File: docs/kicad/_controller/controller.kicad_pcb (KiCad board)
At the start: 2 copper layers, 134.6 x 104.1 mm, 88 parts, among them J1 24V, J10 bbb, J11 Y, J12 X_ZERO, J13 Z, J14 WS2812B Strip, J15 Display, J16 X_LIM, J17 Y_ZERO, J18 Y_LIM, J19 Z_ZERO, J2 GND, J20 Z_LIM, J21 PROBE, J22 UNUSED, J3 GND, J4 5V, J5 SPIN, J6 bbb, J7 X, J8 bbb, J9 bbb, M1 A4988, M2 A4988, M3 A4988, M4 SD_TYP0, U1 ESP32_DEV_0, U2 74HC165

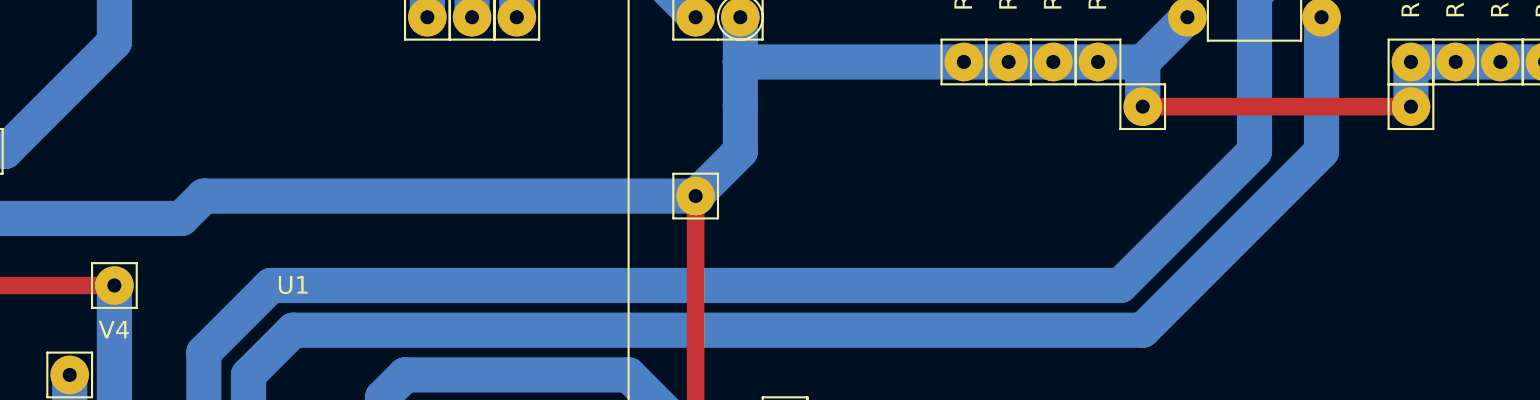
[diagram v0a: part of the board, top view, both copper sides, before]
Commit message: added capacitor and tested I2SI on cnc3018
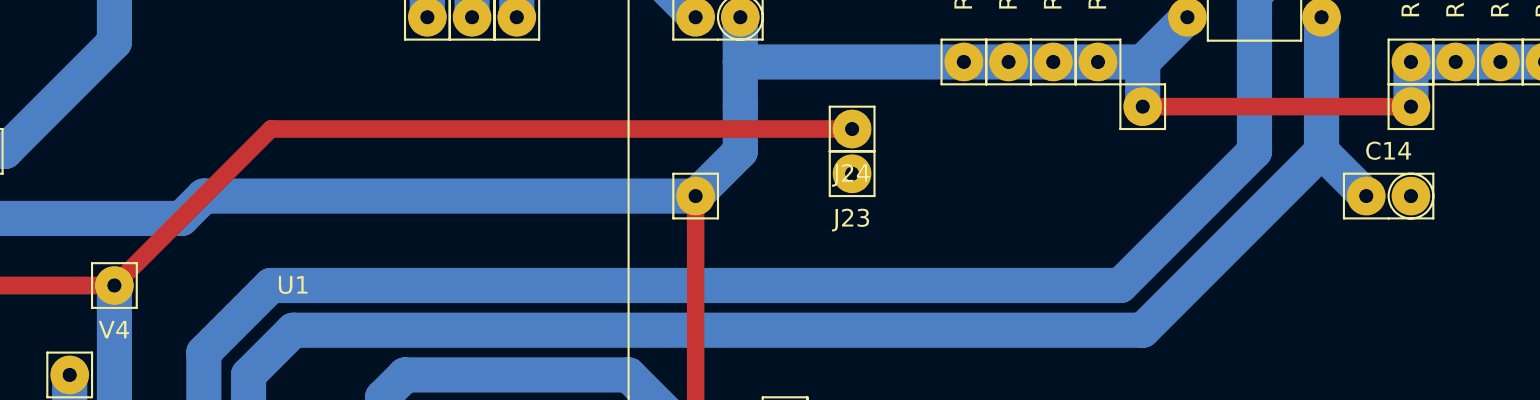
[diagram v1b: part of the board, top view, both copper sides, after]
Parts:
- added C14: 472nf, cnc3018-PCB:my2pin, F.Cu at (116.8, -33.0)
- added J23: GND, cnc3018-PCB:my1pin, F.Cu at (85.1, -34.3)
- added J24: SPIN, cnc3018-PCB:my1pin, F.Cu at (85.1, -36.8)
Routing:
- net Net-(J24-Pad1): track 78.3 -> 123.9 mm
- net Net-(C14-Pad2): track 76.4 -> 80.0 mm

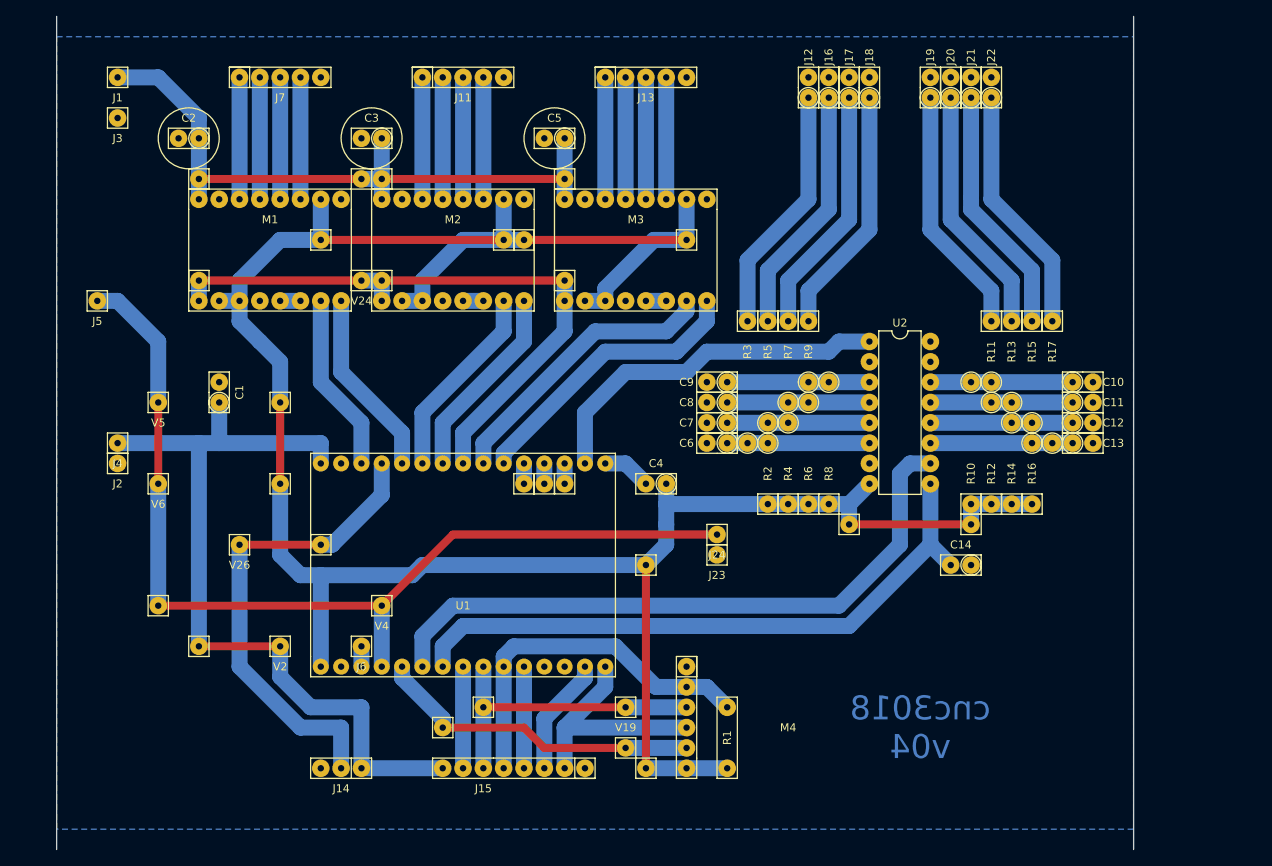
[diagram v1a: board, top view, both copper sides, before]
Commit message: kicad controller board v2.0 and smaller lcd_connector
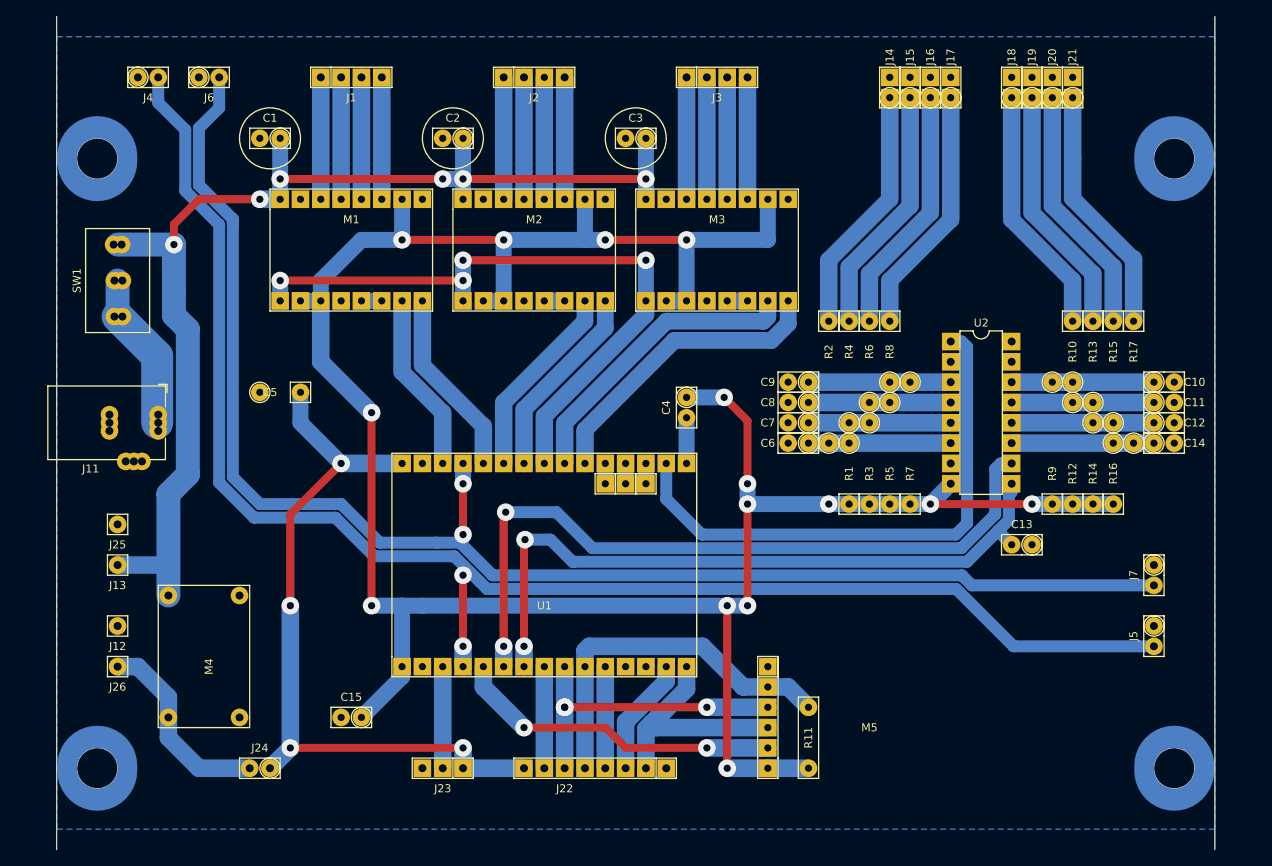
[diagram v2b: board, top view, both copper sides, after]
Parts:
- removed V1: v30, cnc3018-PCB:my1pin
- removed V10: v17, cnc3018-PCB:my1pin
- removed V11: v18, cnc3018-PCB:my1pin
- removed V12: v19, cnc3018-PCB:my1pin
- removed V13: v10, cnc3018-PCB:my1pin
- removed V14: v00, cnc3018-PCB:my1pin
- removed V15: v20, cnc3018-PCB:my1pin
- removed V16: v60, cnc3018-PCB:my1pin
- removed V17: v61, cnc3018-PCB:my1pin
- removed V18: v70, cnc3018-PCB:my1pin
- removed V19: v71, cnc3018-PCB:my1pin
- removed V2: v31, cnc3018-PCB:my1pin
- removed V20: v01, cnc3018-PCB:my1pin
- removed V21: v11, cnc3018-PCB:my1pin
- removed V22: v12, cnc3018-PCB:my1pin
- removed V23: v02, cnc3018-PCB:my1pin
- removed V24: v21, cnc3018-PCB:my1pin
- removed V25: v22, cnc3018-PCB:my1pin
- removed V26: v50, cnc3018-PCB:my1pin
- removed V27: v51, cnc3018-PCB:my1pin
- removed V28: v13, cnc3018-PCB:my1pin
- removed V29: v23, cnc3018-PCB:my1pin
- removed V3: v40, cnc3018-PCB:my1pin
- removed V30: v03, cnc3018-PCB:my1pin
- removed V4: v41, cnc3018-PCB:my1pin
- removed V5: v42, cnc3018-PCB:my1pin
- removed V6: v43, cnc3018-PCB:my1pin
- removed V7: v14, cnc3018-PCB:my1pin
- removed V8: v15, cnc3018-PCB:my1pin
- removed V9: v16, cnc3018-PCB:my1pin
- added C15: 220uf 10V, cnc3018-PCB:my2pin, F.Cu at (40.6, -14.0)
- added J25: bbb, cnc3018-PCB:my1pin, F.Cu at (10.2, -38.1)
- added J26: bbb, cnc3018-PCB:my1pin, F.Cu at (10.2, -20.3)
- added M5: SD_TYP0, cnc3018-PCB:my6Pin, F.Cu at (91.4, -20.3)
- added SW1: POWER, cnc3018-PCB:SW_DPDT_BLUE_LEVER, F.Cu at (10.2, -68.6)
- C1: value 33uf -> 100uf
- C13: value 100nf -> 472nf
- C14: value 472nf -> 100nf
- C5: value 100uf -> 330uf 50v; footprint cnc3018-PCB:my2pin -> cnc3018-PCB:mySkip1
- J1: value 24V -> X_AXIS; footprint cnc3018-PCB:my1pin -> cnc3018-PCB:my4pin
- J11: value Y -> Jack-DC; footprint cnc3018-PCB:my5Pin -> cnc3018-PCB:myBarrelJack
- J12: value X_ZERO -> bbb; footprint cnc3018-PCB:my2pin -> cnc3018-PCB:my1pin
- J13: value Z -> bbb; footprint cnc3018-PCB:my5Pin -> cnc3018-PCB:my1pin
- J14: value WS2812B Strip -> X_ZERO; footprint cnc3018-PCB:my3pin -> cnc3018-PCB:my2pin
- J15: value Display -> X_LIM; footprint cnc3018-PCB:my8Pin -> cnc3018-PCB:my2pin
- J16: value X_LIM -> Y_ZERO
- J17: value Y_ZERO -> Y_LIM
- J18: value Y_LIM -> Z_ZERO
- J19: value Z_ZERO -> Z_LIM
- J2: value GND -> Y_AXIS; footprint cnc3018-PCB:my1pin -> cnc3018-PCB:my4pin
- J20: value Z_LIM -> PROBE
- J21: value PROBE -> UNUSED
- J22: value UNUSED -> Display; footprint cnc3018-PCB:my2pin -> cnc3018-PCB:my8Pin
- J23: value GND -> WS2812B Strip; footprint cnc3018-PCB:my1pin -> cnc3018-PCB:my3pin
- J24: value SPIN -> 5V Jumper; footprint cnc3018-PCB:my1pin -> cnc3018-PCB:my2pin
- J3: value GND -> Z_AXIS; footprint cnc3018-PCB:my1pin -> cnc3018-PCB:my4pin
- J4: value 5V -> PWM_1A; footprint cnc3018-PCB:my1pin -> cnc3018-PCB:my2pin
- J5: value SPIN -> PWM_1B; footprint cnc3018-PCB:my1pin -> cnc3018-PCB:my2pin
- J6: value bbb -> PWM_2A; footprint cnc3018-PCB:my1pin -> cnc3018-PCB:my2pin
- J7: value X -> PWM_2B; footprint cnc3018-PCB:my5Pin -> cnc3018-PCB:my2pin
- M4: value SD_TYP0 -> BUCK01; footprint cnc3018-PCB:my6Pin -> cnc3018-PCB:BUCK01
- R1: footprint cnc3018-PCB:myResistor -> cnc3018-PCB:mySkip2
- R10, R8: value 10K -> 100; footprint cnc3018-PCB:mySkip5 -> cnc3018-PCB:mySkip2
- R11: value 100 -> 10K; footprint cnc3018-PCB:mySkip2 -> cnc3018-PCB:myResistor
- R2: value 10K -> 100; footprint cnc3018-PCB:mySkip2 -> cnc3018-PCB:mySkip5
- R3: value 100 -> 10K; footprint cnc3018-PCB:mySkip5 -> cnc3018-PCB:mySkip3
- R4: value 10K -> 100; footprint cnc3018-PCB:mySkip3 -> cnc3018-PCB:mySkip4
- R5: value 100 -> 10K
- R6: value 10K -> 100; footprint cnc3018-PCB:mySkip4 -> cnc3018-PCB:mySkip3
- R7: value 100 -> 10K; footprint cnc3018-PCB:mySkip3 -> cnc3018-PCB:mySkip5
- R9: value 100 -> 10K; footprint cnc3018-PCB:mySkip2 -> cnc3018-PCB:mySkip5
- moved J5 138.2 mm to (139.7, -25.4), turned to 270 degrees
- moved J7 125.1 mm to (139.7, -33.0), turned to 270 degrees
- moved J12 108.7 mm to (10.2, -25.4), turned to 0 degrees
- moved J14 108.3 mm to (106.7, -91.4), turned to 90 degrees
- moved J15 96.7 mm to (109.2, -91.4), turned to 90 degrees
- moved J22 96.7 mm to (71.1, -7.62), turned to 180 degrees
- moved J13 89.9 mm to (10.2, -33.0)
- moved J6 74.0 mm to (20.3, -94.0)
- moved J3 71.3 mm to (81.3, -94.0)
- moved J2 68.2 mm to (58.4, -94.0)
- moved J24 63.1 mm to (29.2, -7.62), turned to 180 degrees
- moved R11 60.4 mm to (96.5, -7.62), turned to 90 degrees
- moved J11 57.6 mm to (15.2, -50.8)
- moved M4 56.0 mm to (25.4, -24.1)
- moved C5 45.8 mm to (33.0, -54.6)
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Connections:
- net Net-(M1-Pad1) renamed X_DIR
- net Net-(M1-Pad2) renamed X_STEP
- net Net-(M1-Pad8) renamed STEP_EN
- net Net-(M2-Pad1) renamed Y_DIR
- net Net-(M2-Pad2) renamed Y_STEP
- net Net-(M3-Pad1) renamed Z_DIR
- net Net-(M3-Pad2) renamed Z_STEP
- net Net-(U1-Pad14) renamed SW_DATA
- net Net-(U1-Pad25) renamed SW_CLK
- C1 pad 1: Net-(C1-Pad1) -> +24V
- C1 pad 2: Net-(C1-Pad2) -> GND
- C10 pad 2: Net-(C1-Pad2) -> GND
- C11 pad 2: Net-(C1-Pad2) -> GND
- C12 pad 2: Net-(C1-Pad2) -> GND
- C13 pad 1: Net-(C13-Pad1) -> GND
- C13 pad 2: Net-(C1-Pad2) -> SW_LATCH
- C14 pad 1: Net-(C1-Pad2) -> Net-(C14-Pad1)
- C14 pad 2: Net-(C14-Pad2) -> GND
- C2 pad 1: Net-(C2-Pad1) -> +24V
- C2 pad 2: Net-(C1-Pad2) -> GND
- C3 pad 1: Net-(C2-Pad1) -> +24V
- C3 pad 2: Net-(C1-Pad2) -> GND
- C4 pad 1: Net-(C4-Pad1) -> +3V3
- C5 pad 1: Net-(C2-Pad1) -> +5V
- C5 pad 2: Net-(C1-Pad2) -> GND
- C6 pad 2: Net-(C1-Pad2) -> GND
- C7 pad 2: Net-(C1-Pad2) -> GND
- C8 pad 2: Net-(C1-Pad2) -> GND
- C9 pad 2: Net-(C1-Pad2) -> GND
- J1 pad 1: Net-(C2-Pad1) -> Net-(J1-Pad1)
- J11 pad 2: Net-(J11-Pad2) -> GND
- J11 pad 3: Net-(J11-Pad3) -> (no net)
- J12 pad 1: Net-(J12-Pad1) -> GND
- J13 pad 1: Net-(J13-Pad1) -> +24V
- J14 pad 1: Net-(C1-Pad1) -> Net-(J14-Pad1)
- J14 pad 2: Net-(J14-Pad2) -> GND
- J15 pad 1: Net-(C1-Pad2) -> Net-(J15-Pad1)
- J15 pad 2: Net-(J15-Pad2) -> GND
- J16 pad 2: Net-(C1-Pad2) -> GND
- J17 pad 2: Net-(C1-Pad2) -> GND
- J18 pad 2: Net-(C1-Pad2) -> GND
- J19 pad 2: Net-(C1-Pad2) -> GND
- J2 pad 1: Net-(C1-Pad2) -> Net-(J2-Pad1)
- J20 pad 2: Net-(C1-Pad2) -> GND
- J21 pad 2: Net-(C1-Pad2) -> GND
- J22 pad 1: Net-(J22-Pad1) -> GND
- J22 pad 2: Net-(C1-Pad2) -> MOSI
- J23 pad 1: Net-(C1-Pad2) -> +5V
- J24 pad 1: Net-(J24-Pad1) -> +5V
- J3 pad 1: Net-(C1-Pad2) -> Net-(J3-Pad1)
- J4 pad 1: Net-(C1-Pad1) -> GND
- J5 pad 1: Net-(J24-Pad1) -> GND
- J6 pad 1: Net-(J6-Pad1) -> GND
- J7 pad 1: Net-(J7-Pad1) -> GND
- J7 pad 2: Net-(J7-Pad2) -> PWM_2
- M1 pad 10: Net-(C1-Pad2) -> GND
- M1 pad 11: Net-(J7-Pad1) -> Net-(J1-Pad1)
- M1 pad 12: Net-(J7-Pad2) -> Net-(J1-Pad2)
- M1 pad 13: Net-(J7-Pad3) -> Net-(J1-Pad3)
- M1 pad 14: Net-(J7-Pad4) -> Net-(J1-Pad4)
- M1 pad 15: Net-(C4-Pad1) -> +3V3
- M1 pad 16: Net-(C1-Pad2) -> GND
- M1 pad 6: Net-(C4-Pad1) -> +3V3
- M1 pad 7: Net-(C4-Pad1) -> +3V3
- M1 pad 9: Net-(C2-Pad1) -> +24V
- M2 pad 10: Net-(C1-Pad2) -> GND
- M2 pad 11: Net-(J11-Pad1) -> Net-(J2-Pad1)
- M2 pad 12: Net-(J11-Pad2) -> Net-(J2-Pad2)
- M2 pad 13: Net-(J11-Pad3) -> Net-(J2-Pad3)
- M2 pad 14: Net-(J11-Pad4) -> Net-(J2-Pad4)
- M2 pad 15: Net-(C4-Pad1) -> +3V3
- M2 pad 16: Net-(C1-Pad2) -> GND
- M2 pad 6: Net-(C4-Pad1) -> +3V3
- M2 pad 7: Net-(C4-Pad1) -> +3V3
- M2 pad 9: Net-(C2-Pad1) -> +24V
- M3 pad 10: Net-(C1-Pad2) -> GND
- M3 pad 11: Net-(J13-Pad1) -> Net-(J3-Pad1)
- M3 pad 12: Net-(J13-Pad2) -> Net-(J3-Pad2)
- M3 pad 13: Net-(J13-Pad3) -> Net-(J3-Pad3)
- M3 pad 14: Net-(J13-Pad4) -> Net-(J3-Pad4)
- M3 pad 15: Net-(C4-Pad1) -> +3V3
- M3 pad 16: Net-(C1-Pad2) -> GND
- M3 pad 6: Net-(C4-Pad1) -> +3V3
- M3 pad 7: Net-(C4-Pad1) -> +3V3
- M3 pad 9: Net-(C2-Pad1) -> +24V
- M4 pad 1: Net-(C1-Pad2) -> GND
- M4 pad 2: Net-(J15-Pad5) -> GND
- M4 pad 3: Net-(J15-Pad6) -> Net-(J24-Pad2)
- M4 pad 4: Net-(J15-Pad2) -> +24V
- R1 pad 1: Net-(C4-Pad1) -> +3V3
- R1 pad 2: Net-(J15-Pad5) -> Net-(C6-Pad1)
- R10 pad 1: Net-(C4-Pad1) -> Net-(J18-Pad1)
- R11 pad 1: Net-(J19-Pad1) -> +3V3
- R11 pad 2: Net-(C10-Pad1) -> MISO
- R12 pad 1: Net-(C4-Pad1) -> +3V3
- R13 pad 1: Net-(J20-Pad1) -> Net-(J19-Pad1)
- R14 pad 1: Net-(C4-Pad1) -> +3V3
- R15 pad 1: Net-(J21-Pad1) -> Net-(J20-Pad1)
- R16 pad 1: Net-(C4-Pad1) -> +3V3
- R16 pad 2: Net-(C13-Pad1) -> Net-(C14-Pad1)
- R17 pad 1: Net-(J22-Pad1) -> Net-(J21-Pad1)
- R17 pad 2: Net-(C13-Pad1) -> Net-(C14-Pad1)
- R2 pad 1: Net-(C4-Pad1) -> Net-(J14-Pad1)
- R3 pad 1: Net-(J12-Pad1) -> +3V3
- R3 pad 2: Net-(C6-Pad1) -> Net-(C7-Pad1)
- R4 pad 1: Net-(C4-Pad1) -> Net-(J15-Pad1)
- R5 pad 1: Net-(J16-Pad1) -> +3V3
- R5 pad 2: Net-(C7-Pad1) -> Net-(C8-Pad1)
- R6 pad 1: Net-(C4-Pad1) -> Net-(J16-Pad1)
- R7 pad 1: Net-(J17-Pad1) -> +3V3
- R7 pad 2: Net-(C8-Pad1) -> Net-(C9-Pad1)
- R8 pad 1: Net-(C4-Pad1) -> Net-(J17-Pad1)
- R9 pad 1: Net-(J18-Pad1) -> +3V3
- R9 pad 2: Net-(C9-Pad1) -> Net-(C10-Pad1)
- U1 pad 1: Net-(C1-Pad1) -> +5V
- U1 pad 16: Net-(J15-Pad2) -> MOSI
- U1 pad 17: Net-(J15-Pad3) -> TFT_CS
- U1 pad 2: Net-(C1-Pad2) -> GND
- U1 pad 20: Net-(J15-Pad4) -> TFT_DC
- U1 pad 21: Net-(J15-Pad5) -> MISO
- U1 pad 22: Net-(J15-Pad6) -> MCLK
- U1 pad 23: Net-(J15-Pad7) -> TOUCH_CS
- U1 pad 24: Net-(C14-Pad2) -> SW_LATCH
- U1 pad 26: Net-(M4-Pad5) -> SD_CS
- U1 pad 27: Net-(J24-Pad1) -> PWM_1
- U1 pad 28: Net-(J6-Pad1) -> LED
- U1 pad 29: Net-(C1-Pad2) -> GND
- U1 pad 30: Net-(C4-Pad1) -> +3V3
- U1 pad 4: Net-(J14-Pad2) -> PWM_2
- U2 pad 11: Net-(C13-Pad1) -> Net-(C14-Pad1)
- U2 pad 16: Net-(C1-Pad2) -> GND
- U2 pad 2: Net-(C1-Pad2) -> GND
- U2 pad 7: Net-(C1-Pad2) -> GND
- U2 pad 8: Net-(C4-Pad1) -> +3V3
- U2 pad 9: Net-(C14-Pad2) -> SW_LATCH
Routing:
- net +3V3: track 0.00 -> 314.2 mm, vias 0 -> 15
- net Net-(C4-Pad1): track 306.2 -> 0.00 mm
- net PWM_1: track 0.00 -> 192.1 mm, vias 0 -> 2
- net PWM_2: track 0.00 -> 184.3 mm, vias 0 -> 2
- net +24V: track 0.00 -> 143.4 mm, vias 0 -> 6
- net Net-(J24-Pad1): track 123.9 -> 0.00 mm
- net Net-(C1-Pad1): track 101.9 -> 0.00 mm
- net +5V: track 0.00 -> 92.1 mm, vias 0 -> 4
- net SW_LATCH: track 0.00 -> 86.8 mm, vias 0 -> 2
- net Net-(C2-Pad1): track 83.4 -> 0.00 mm
- net Net-(C14-Pad2): track 80.0 -> 0.00 mm
- net Net-(J14-Pad2): track 60.5 -> 0.00 mm
- net MISO: track 0.00 -> 46.0 mm
- net Net-(J15-Pad5): track 45.6 -> 0.00 mm
- net Net-(M4-Pad5): track 41.3 -> 0.00 mm
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- added copper zone on B.Cu, net GND
- removed copper zone on B.Cu, net Net-(C1-Pad2)
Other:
- board size 134.6 x 104.1 mm -> 144.8 x 104.1 mm
- board text added: "cnc3018 v2.0 Patrick Horton"
- board text removed: "cnc3018 v04"

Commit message: version 2 PCB and smaller LCD connector
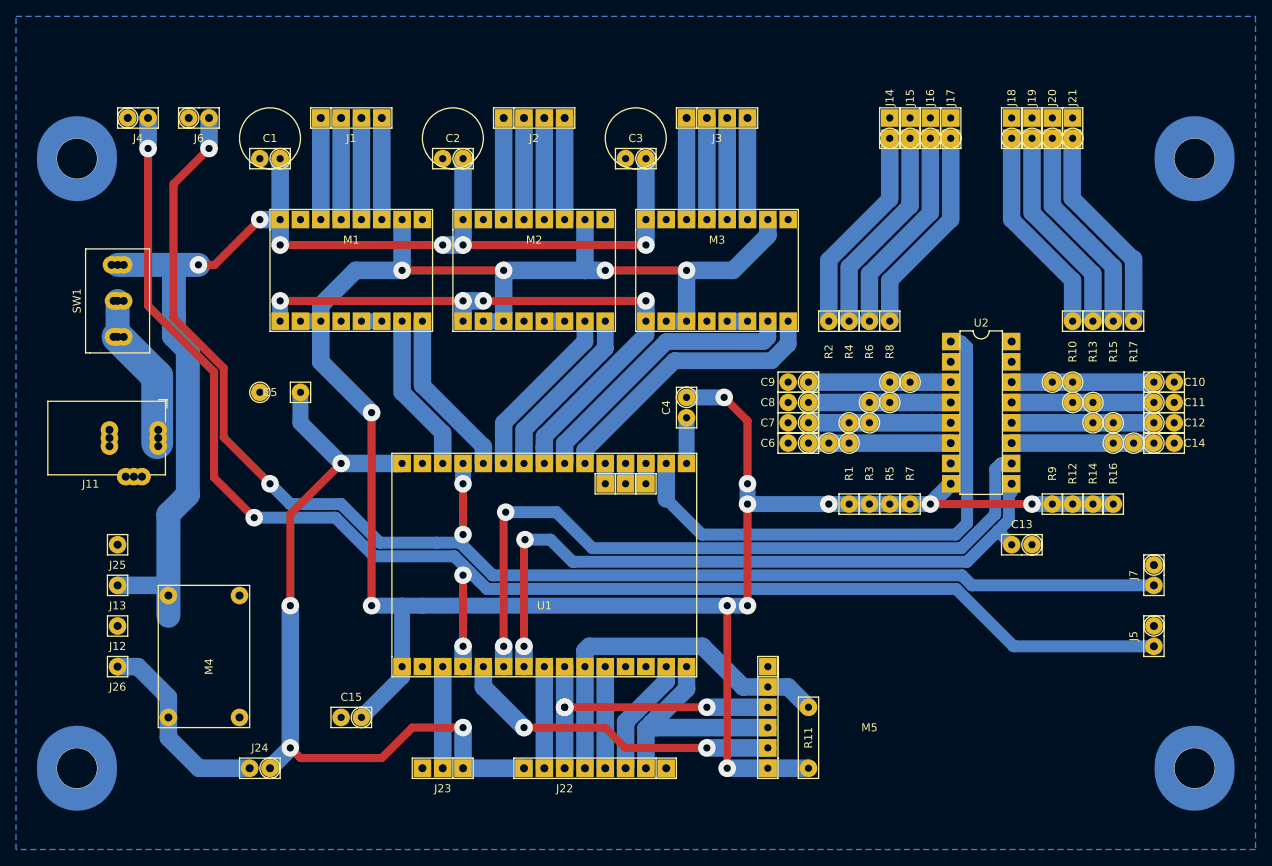
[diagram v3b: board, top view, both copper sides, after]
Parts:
- moved J4 5.24 mm to (11.4, -88.9)
- moved J6 5.24 mm to (19.1, -88.9)
- moved J1 5.08 mm to (35.6, -88.9)
- moved J14 5.08 mm to (106.7, -86.4)
- moved J15 5.08 mm to (109.2, -86.4)
- moved J16 5.08 mm to (111.8, -86.4)
- moved J17 5.08 mm to (114.3, -86.4)
- moved J18 5.08 mm to (121.9, -86.4)
- moved J19 5.08 mm to (124.5, -86.4)
- moved J2 5.08 mm to (58.4, -88.9)
- moved J20 5.08 mm to (127.0, -86.4)
- moved J21 5.08 mm to (129.5, -86.4)
- moved J3 5.08 mm to (81.3, -88.9)
- moved C1 2.54 mm to (30.5, -83.8)
- moved C2 2.54 mm to (53.3, -83.8)
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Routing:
- net +24V: track 143.4 -> 151.4 mm
- net STEP_EN: track 84.0 -> 76.4 mm
- net PWM_2: track 184.3 -> 178.4 mm, vias 2 -> 4
- net Net-(J20-Pad1): track 31.1 -> 26.0 mm
- net Net-(J19-Pad1): track 31.1 -> 26.0 mm
- net Net-(J18-Pad1): track 31.1 -> 26.0 mm
- net Net-(J17-Pad1): track 31.1 -> 26.0 mm
- net Net-(J15-Pad1): track 31.3 -> 26.2 mm
- net Net-(J14-Pad1): track 31.1 -> 26.0 mm
- net Net-(J16-Pad1): track 31.3 -> 26.2 mm
- net Net-(J21-Pad1): track 31.1 -> 26.1 mm
- net +3V3: track 314.2 -> 309.5 mm
- net +5V: track 92.1 -> 96.8 mm
- net PWM_1: track 192.1 -> 187.5 mm, vias 2 -> 4
- net Z_STEP: track 38.0 -> 35.4 mm
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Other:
- board outline removed
- board text added: "cnc3018 v2.1 Patrick Horton March 2022"
- board text removed: "cnc3018 v2.0 Patrick Horton"

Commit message: working on CNC_3018 v2
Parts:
- R1: value 10K -> 6.8K actual
- R2: value 100 -> 220 Actual
